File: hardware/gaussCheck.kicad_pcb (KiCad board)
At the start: 2 copper layers, 42 parts, among them J1 USB_C_Receptacle_USB2.0, J2 SWD, SW1 PTS810, SW2 CK KSC2, SW3 CK KSC2, SW4 CK KSC2, U1 TLV493D, U2 VIM-878-DP, U3 ATSAML22N18A-AUT, U4 TPS613221ADBV, Y1 32.768kHz

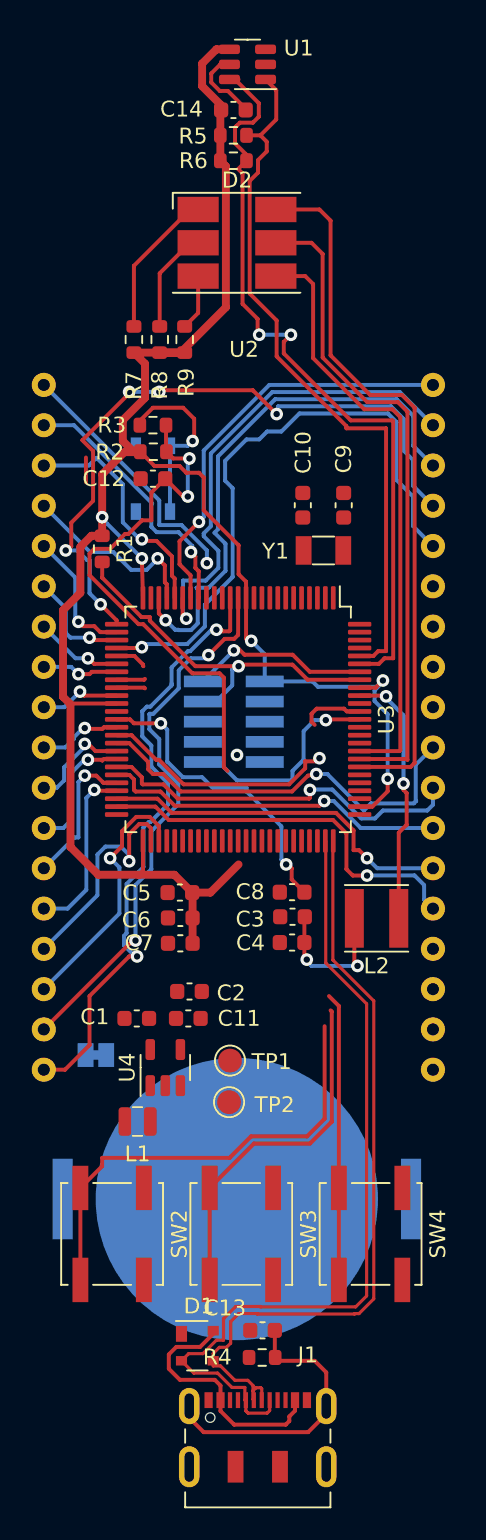
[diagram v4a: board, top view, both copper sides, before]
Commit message: change btn in sch, routing
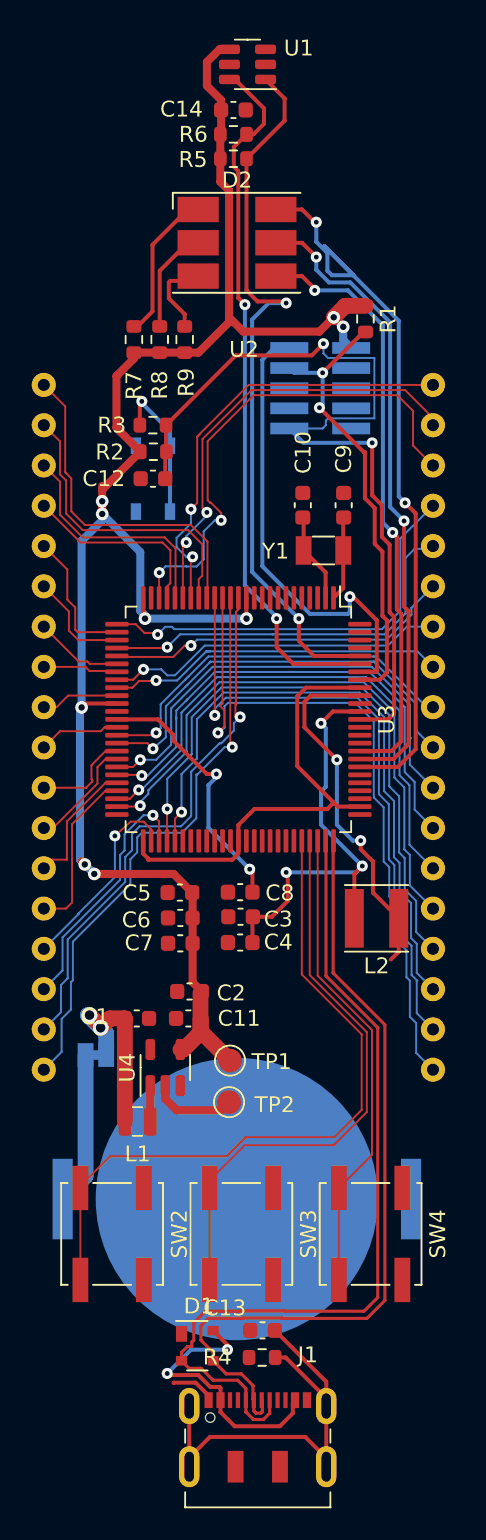
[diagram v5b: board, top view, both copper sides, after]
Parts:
- moved R1 22.0 mm to (149.6, 68.9)
- moved J2 21.7 mm to (146.8, 73.3)
- moved C3 3.28 mm to (141.7, 106.6)
- moved C4 3.28 mm to (141.7, 108.2)
- moved C8 3.28 mm to (141.7, 105.0)
- moved R6 1.66 mm to (141.3, 57.3)
- moved R5 1.47 mm to (141.3, 58.8)
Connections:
- U3 pad 3: /MCU/BTN1 -> unconnected-(U3C-PC00/I8/AIN16-Pad3)
- U3 pad 4: /MCU/BTN2 -> unconnected-(U3C-PC01/I9/AIN17-Pad4)
- U3 pad 5: /MCU/BTN3 -> unconnected-(U3C-PC02/I10/AIN18-Pad5)
- U3 pad 71: unconnected-(U3A-PA21/SLCD[49]-Pad71) -> /MCU/BTN1
- U3 pad 72: unconnected-(U3A-PA22/SERCOM0.2|2.0|I2C/SLCD[50]-Pad72) -> /MCU/BTN2
- U3 pad 73: unconnected-(U3A-PA23/SERCOM0.3|2.1|I2C/SLCD[51]-Pad73) -> /MCU/BTN3
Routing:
- net /MCU/COM2: track 0.00 -> 44.3 mm, vias 0 -> 1
- net /MCU/DPCBA8: track 0.00 -> 40.1 mm, vias 0 -> 1
- net /MCU/COM3: track 0.00 -> 40.0 mm, vias 0 -> 1
- net /MCU/MNGH8: track 0.00 -> 38.6 mm, vias 0 -> 1
- net /MCU/DPCBA3: track 2.00 -> 22.2 mm, vias 0 -> 1
- net /MCU/DPCBA4: track 1.81 -> 21.8 mm, vias 0 -> 1
- net /MCU/MNGH4: track 1.81 -> 21.6 mm, vias 0 -> 1
- net /MCU/DPCBA2: track 44.7 -> 26.5 mm, vias 5 -> 1
- net /MCU/SWDIO: track 11.3 -> 29.4 mm
- net /MCU/MNGH3: track 40.2 -> 24.9 mm
- net +3V3: track 129.2 -> 144.3 mm, vias 5 -> 9
- net /MCU/BTN1: track 29.2 -> 44.2 mm
- net /MCU/BTN2: track 22.3 -> 36.6 mm
- net Net-(U3D-VDDCORE): track 13.7 -> 27.9 mm, vias 2 -> 3
- net /Bat: track 0.00 -> 12.5 mm, vias 0 -> 2
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
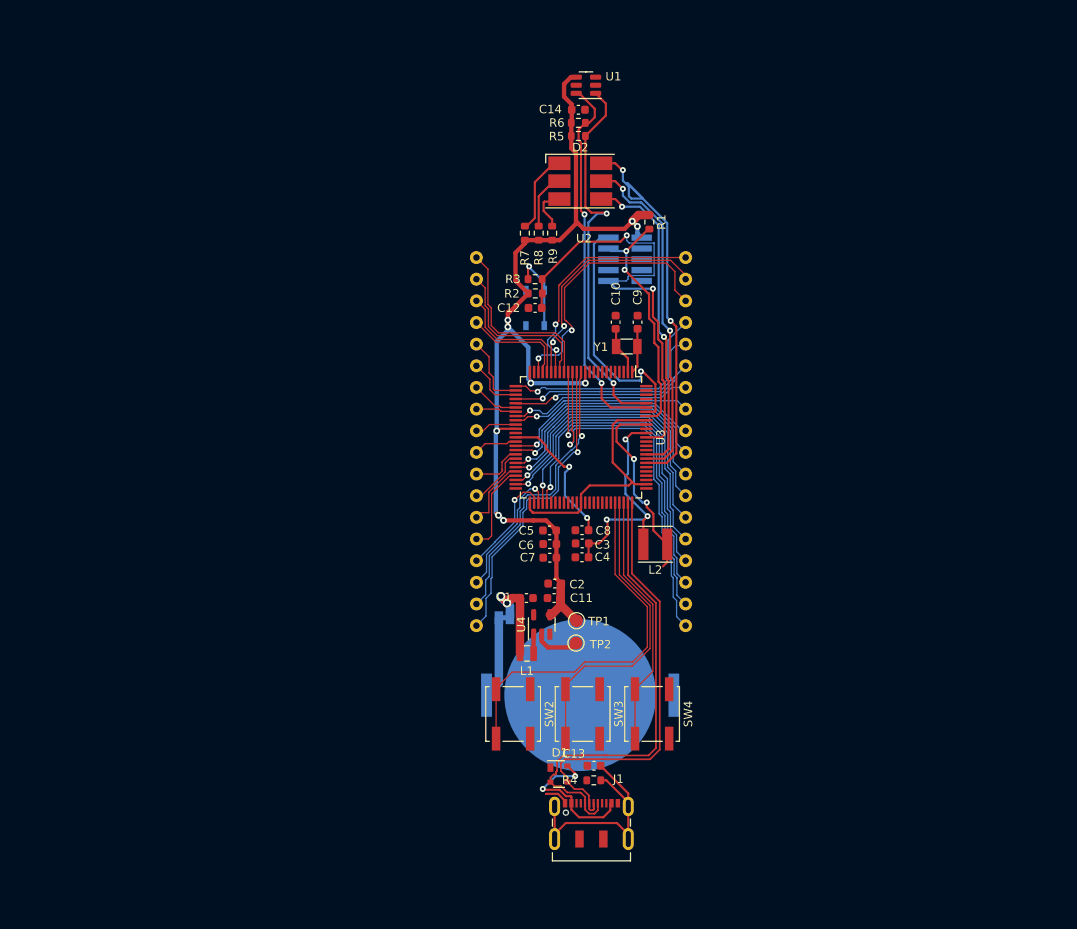
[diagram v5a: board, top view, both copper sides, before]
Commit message: added 3Dmodel for Display centered and locked key components
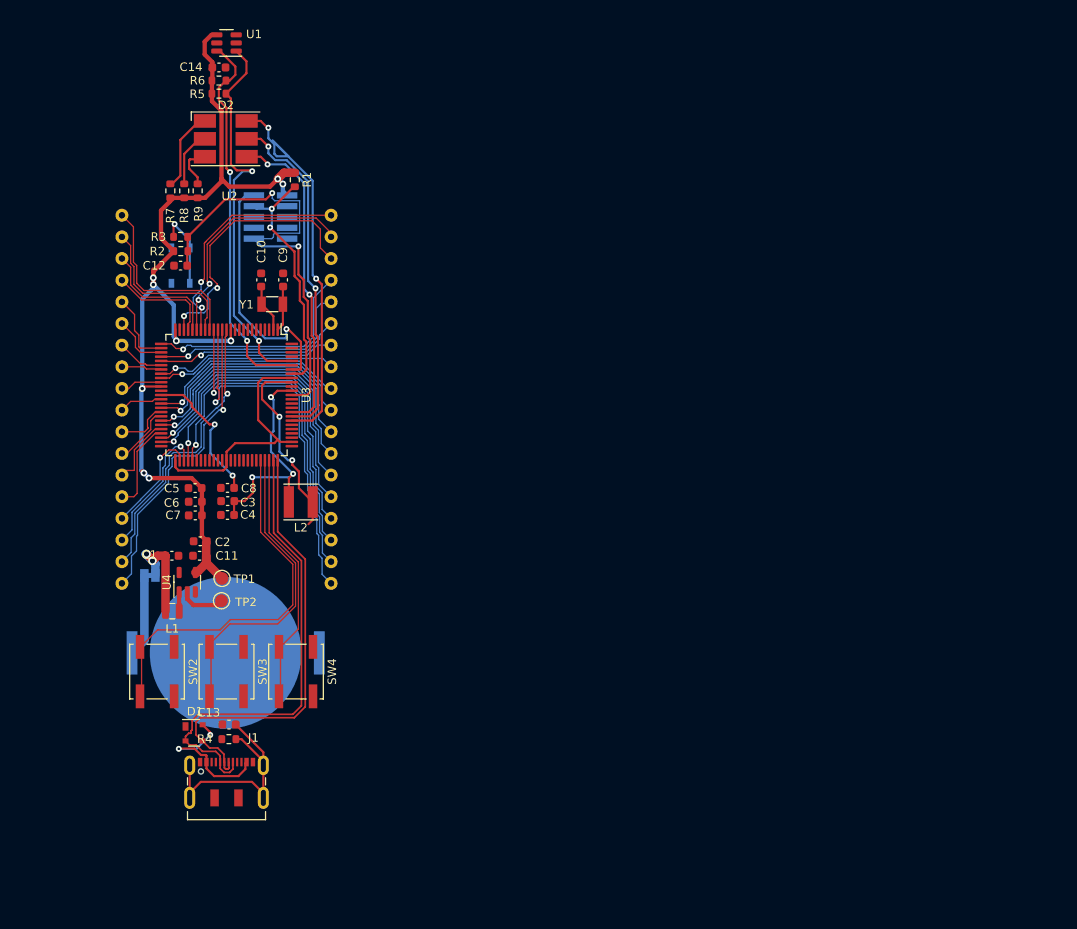
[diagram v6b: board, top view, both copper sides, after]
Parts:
- moved C13 43.1 mm to (100.3, 127.8)
- moved D1 43.1 mm to (96.2, 128.8)
- moved J1 43.1 mm to (100.0, 135.3)
- moved R4 43.1 mm to (100.3, 129.6)
- moved C14 42.5 mm to (99.1, 50.8)
- moved R5 42.5 mm to (99.1, 53.8)
- moved R6 42.5 mm to (99.1, 52.3)
- moved U1 42.5 mm to (100.0, 47.9)
- moved SW2 42.1 mm to (91.8, 121.6)
- moved SW3 42.1 mm to (100.0, 121.6)
- moved SW4 42.1 mm to (108.2, 121.6)
- moved BT1 41.9 mm to (99.9, 119.4)
- moved C1 41.9 mm to (93.6, 108.0)
- moved C10 41.9 mm to (104.1, 75.7)
- moved C11 41.9 mm to (96.8, 108.0)
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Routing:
- net GND: track 8.21 -> 5.36 mm
- net /MCU/D-: track 54.3 -> 55.5 mm
- net /MCU/D+: track 51.3 -> 52.5 mm
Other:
- board text added: "Center of Display"

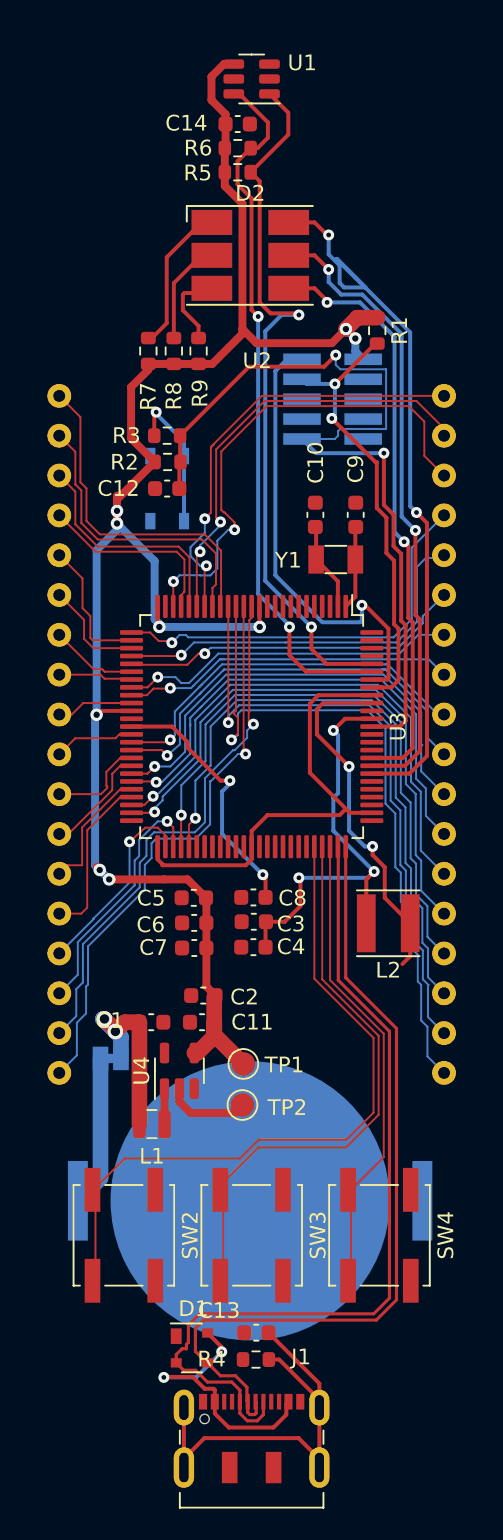
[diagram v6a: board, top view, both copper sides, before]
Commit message: added 3D models to pushbuttons
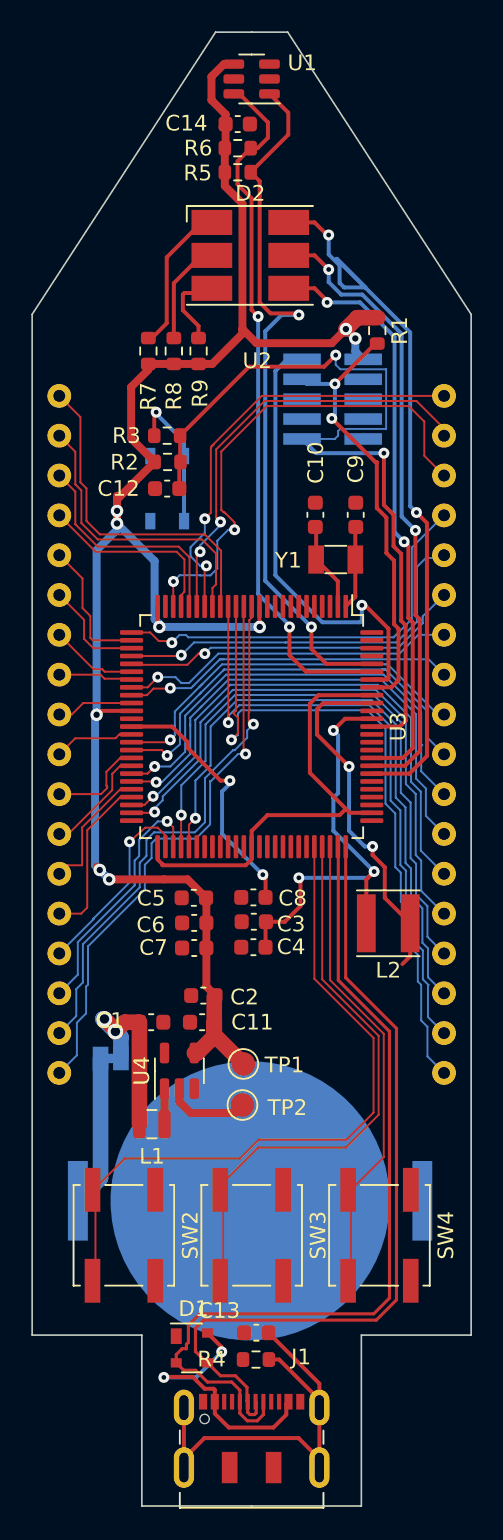
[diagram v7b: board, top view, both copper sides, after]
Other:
- board outline added: 28 x 94 mm
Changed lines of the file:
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@@
+      (rotate (xyz 0 0 0))
+    )
+    (model "${KIPRJMOD}/packages3D/SW_Push_1P1T_NO_CK_KSC7xxJ.wrl"
+      (offset (xyz 0 0 0))
+      (scale (xyz 1 1 1))
       (rotate (xyz 0 0 0))
     )
@@
       (rotate (xyz 0 0 0))
     )
+    (model "${KIPRJMOD}/packages3D/SW_Push_1P1T_NO_CK_KSC7xxJ.wrl"
+      (offset (xyz 0 0 0))
+      (scale (xyz 1 1 1))
+      (rotate (xyz 0 0 0))
+    )
   )
   (footprint "Button_Switch_SMD:SW_Push_1P1T_NO_CK_KSC7xxJ" locked (layer "F.Cu")
@@
       (net 2 "GND") (pinfunction "2") (pintype "passive"))
     (model "${KICAD6_3DMODEL_DIR}/Button_Switch_SMD.3dshapes/SW_push_1P1T_NO_CK_KSC7xxJxxx.wrl"
+      (offset (xyz 0 0 0))
+      (scale (xyz 1 1 1))
+      (rotate (xyz 0 0 0))
+    )
+    (model "${KIPRJMOD}/packages3D/SW_Push_1P1T_NO_CK_KSC7xxJ.wrl"
       (offset (xyz 0 0 0))
       (scale (xyz 1 1 1))
@@
   (gr_line (start 100 34.65) (end 100 152)
     (stroke (width 0.15) (type default)) (layer "Cmts.User"))
+  (gr_line (start 93 128) (end 93 138.9)
+    (stroke (width 0.1) (type default)) (layer "Edge.Cuts"))
+  (gr_line (start 107 138.9) (end 100 138.9)
+    (stroke (width 0.1) (type default)) (layer "Edge.Cuts"))
+  (gr_line (start 100 44.9) (end 102.3 44.9)
+    (stroke (width 0.1) (type default)) (layer "Edge.Cuts"))
+  (gr_line (start 114 128) (end 107 128)
+    (stroke (width 0.1) (type default)) (layer "Edge.Cuts"))
+  (gr_line (start 97.7 44.9) (end 86 62.9)
+    (stroke (width 0.1) (type default)) (layer "Edge.Cuts"))
+  (gr_line (start 100 44.9) (end 97.7 44.9)
+    (stroke (width 0.1) (type default)) (layer "Edge.Cuts"))
+  (gr_line (start 107 128) (end 107 138.9)
+    (stroke (width 0.1) (type default)) (layer "Edge.Cuts"))
+  (gr_line (start 102.3 44.9) (end 114 62.9)
+    (stroke (width 0.1) (type default)) (layer "Edge.Cuts"))
+  (gr_line (start 86 62.9) (end 86 128)
+    (stroke (width 0.1) (type default)) (layer "Edge.Cuts"))
+  (gr_line (start 86 128) (end 93 128)
+    (stroke (width 0.1) (type default)) (layer "Edge.Cuts"))
+  (gr_line (start 114 62.9) (end 114 128)
+    (stroke (width 0.1) (type default)) (layer "Edge.Cuts"))
+  (gr_line (start 93 138.9) (end 100 138.9)
+    (stroke (width 0.1) (type default)) (layer "Edge.Cuts"))
   (gr_text "Center of Display" (at 100.33 152.05) (layer "Cmts.User")
     (effects (font (size 1 1) (thickness 0.15)) (justify left bottom))

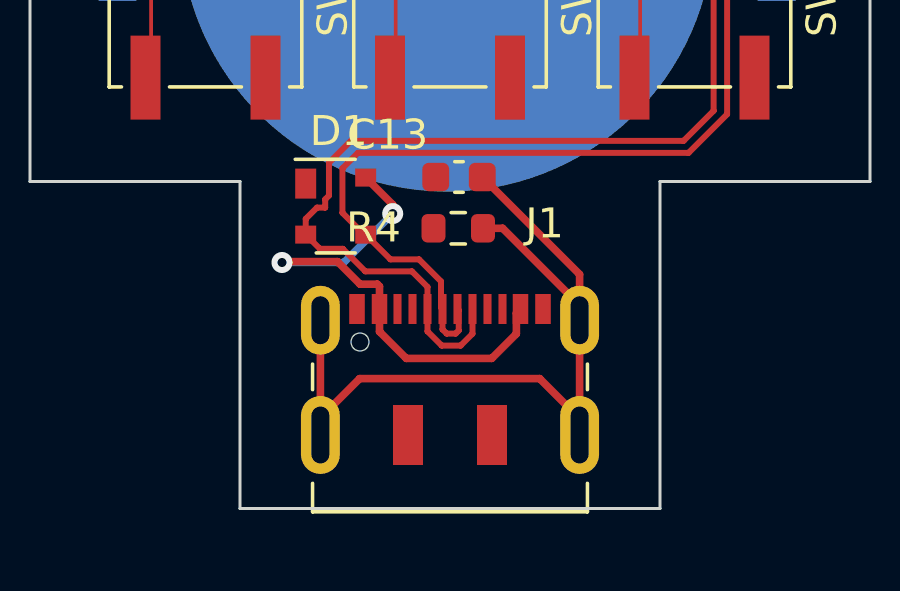
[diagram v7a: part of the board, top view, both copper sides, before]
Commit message: changed USB-C connector to GCT_USB4105 in favor for a 3D model
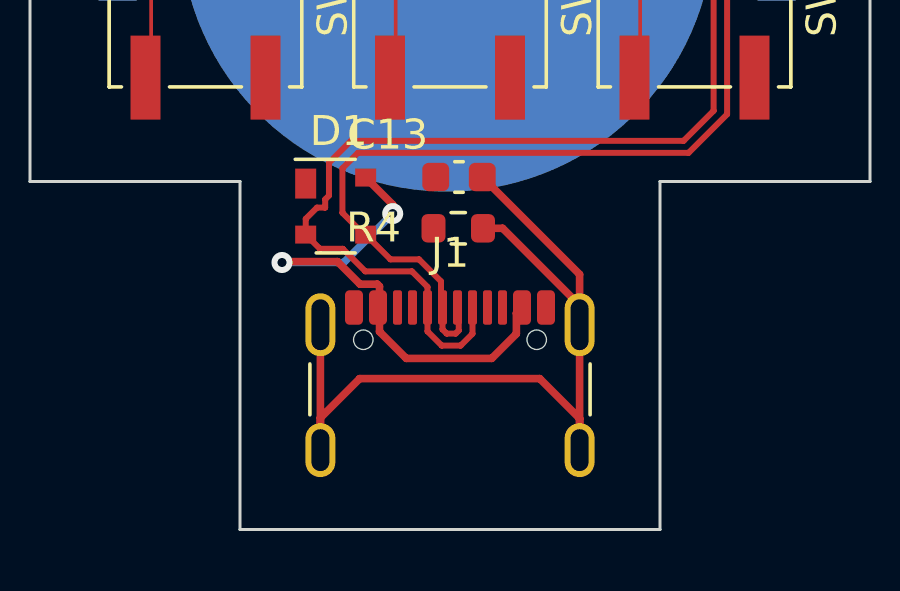
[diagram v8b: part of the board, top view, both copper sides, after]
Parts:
- J1: footprint Connector_USB:USB_C_Receptacle_JAE_DX07S016JA1R1500 -> Connector_USB:USB_C_Receptacle_GCT_USB4105-xx-A_16P_TopMnt_Horizontal
- moved J1 0.58 mm to (100.0, 135.9)
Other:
- board size 28 x 94 mm -> 28 x 94.7 mm
